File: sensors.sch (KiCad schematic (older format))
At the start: 9 parts, among them J3 Screw_Terminal_01x08, J4 Screw_Terminal_01x08, J7 Screw_Terminal_01x02, J8 Conn_01x02_Male, U2 LTC2449CUHF, U4 INA126U

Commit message: completed design 2.0
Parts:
- removed J7: Screw_Terminal_01x02, TerminalBlock_Phoenix:TerminalBlock_Phoenix_MKDS-1,5-2-5.08_1x02_P5.08mm_Horizontal, symbol Connector:Screw_Terminal_01x02
- removed J8: Conn_01x02_Male, Connector_PinHeader_2.54mm:PinHeader_1x02_P2.54mm_Vertical, symbol Connector:Conn_01x02_Male
- added J7: Screw_Terminal_01x04, TerminalBlock_Phoenix:TerminalBlock_Phoenix_MKDS-1,5-4-5.08_1x04_P5.08mm_Horizontal, symbol Connector:Screw_Terminal_01x04
- added J8: Conn_01x03_Male, Connector_PinHeader_2.54mm:PinHeader_1x03_P2.54mm_Vertical, symbol Connector:Conn_01x03_Male
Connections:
- net +EXC: now also J7.1 (Pin_1), J8.1 (Pin_1)
- net GND: now also J7.4 (Pin_4)
- net LC: now also J8.2 (Pin_2)
- net LC+: now also J7.3 (Pin_3)
- net LC-: now also J7.2 (Pin_2)
- net SEN0: now also J8.3 (Pin_3)
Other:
- note added: "Allow shorting LC and SEN0"
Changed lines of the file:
@@
 Text GLabel 7800 2400 0    50   Input ~ 0
 LC-
+Text GLabel 10000 1250 0    50   Input ~ 0
+LC+
+Text GLabel 10000 1150 0    50   Input ~ 0
+LC-
+Text GLabel 10100 2100 0    50   Input ~ 0
++EXC
+Text GLabel 10100 2000 0    50   Input ~ 0
+LC
 $Comp
-L Connector:Screw_Terminal_01x02 J7
-U 1 1 5EEF2437
-P 10250 1150
-F 0 "J7" H 10330 1142 50  0000 L CNN
-F 1 "Screw_Terminal_01x02" H 10330 1051 50  0000 L CNN
-F 2 "TerminalBlock_Phoenix:TerminalBlock_Phoenix_MKDS-1,5-2-5.08_1x02_P5.08mm_Horizontal" H 10250 1150 50  0001 C CNN
-F 3 "~" H 10250 1150 50  0001 C CNN
-	1    10250 1150
+L Connector:Conn_01x03_Male J8
+U 1 1 5EF5E577
+P 10300 2000
+F 0 "J8" H 10272 1932 50  0000 R CNN
+F 1 "Conn_01x03_Male" H 10272 2023 50  0000 R CNN
+F 2 "Connector_PinHeader_2.54mm:PinHeader_1x03_P2.54mm_Vertical" H 10300 2000 50  0001 C CNN
+F 3 "~" H 10300 2000 50  0001 C CNN
+	1    10300 2000
+	-1   0    0    1
+$EndComp
+Text GLabel 10100 1900 0    50   Input ~ 0
+SEN0
+Text Notes 10900 1800 2    50   ~ 0
+Allow shorting LC and SEN0
+$Comp
+L Connector:Screw_Terminal_01x04 J7
+U 1 1 5EF619ED
+P 10200 1150
+F 0 "J7" H 10280 1142 50  0000 L CNN
+F 1 "Screw_Terminal_01x04" H 10280 1051 50  0000 L CNN
+F 2 "TerminalBlock_Phoenix:TerminalBlock_Phoenix_MKDS-1,5-4-5.08_1x04_P5.08mm_Horizontal" H 10200 1150 50  0001 C CNN
+F 3 "~" H 10200 1150 50  0001 C CNN
+	1    10200 1150
 	1    0    0    -1
 $EndComp
-$Comp
-L Connector:Conn_01x02_Male J8
-U 1 1 5EEF4A47
-P 10250 1750
-F 0 "J8" H 10222 1632 50  0000 R CNN
-F 1 "Conn_01x02_Male" H 10222 1723 50  0000 R CNN
-F 2 "Connector_PinHeader_2.54mm:PinHeader_1x02_P2.54mm_Vertical" H 10250 1750 50  0001 C CNN
-F 3 "~" H 10250 1750 50  0001 C CNN
-	1    10250 1750
-	-1   0    0    1
-$EndComp
-Text GLabel 10050 1150 0    50   Input ~ 0
-LC+
-Text GLabel 10050 1250 0    50   Input ~ 0
-LC-
-Text GLabel 10050 1650 0    50   Input ~ 0
+Text GLabel 10000 1050 0    50   Input ~ 0
 +EXC
-Text GLabel 10050 1750 0    50   Input ~ 0
-LC
+Text GLabel 10000 1350 0    50   Input ~ 0
+GND
 $EndSCHEMATC

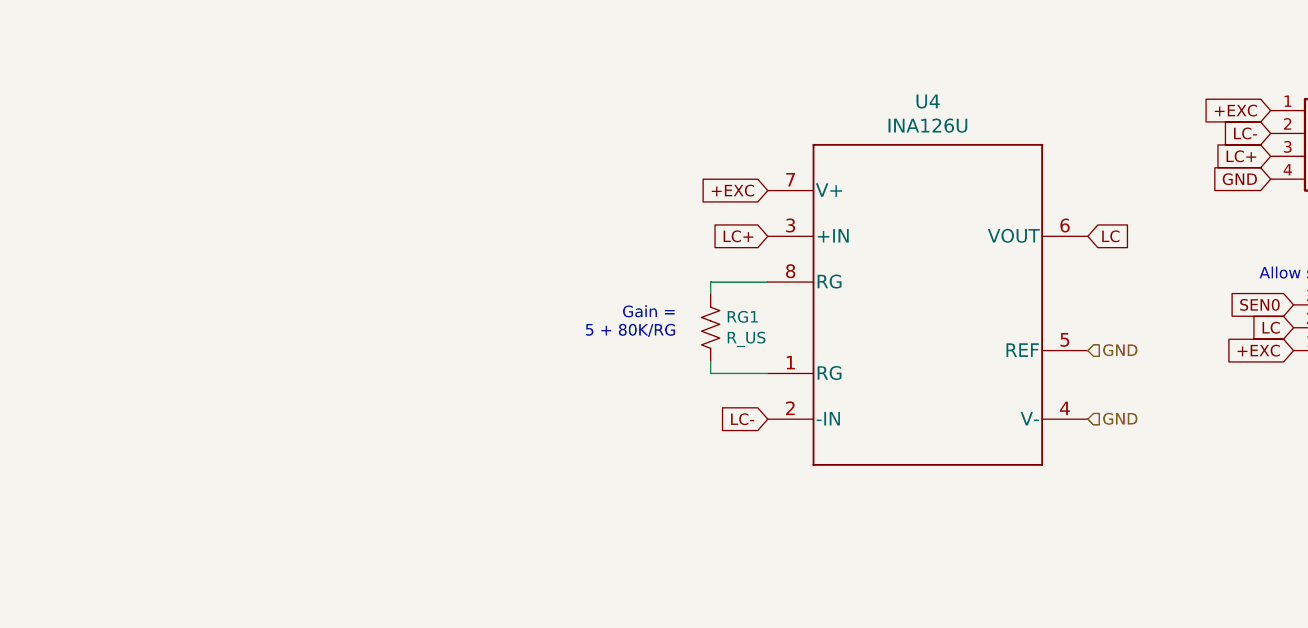
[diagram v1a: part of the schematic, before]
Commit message: added low pass filter to load cell inputs
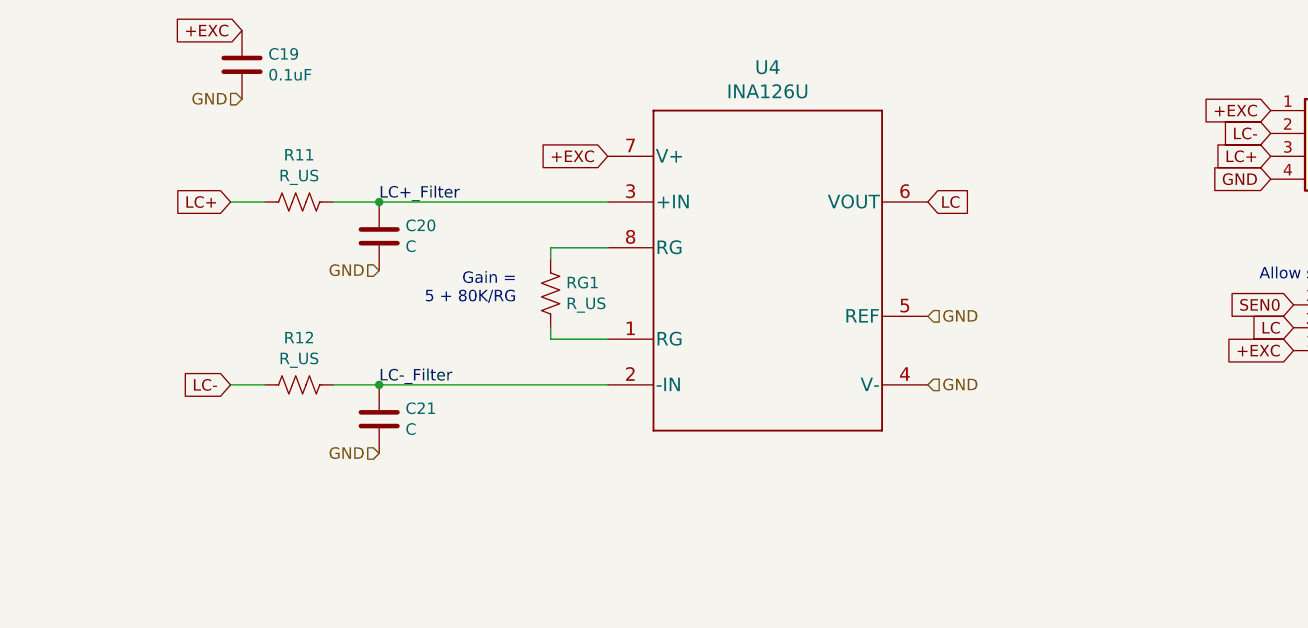
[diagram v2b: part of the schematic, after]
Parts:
- added C19: 0.1uF, Capacitor_SMD:C_0805_2012Metric_Pad1.15x1.40mm_HandSolder, symbol Device:C
- added C20, C21: C, Capacitor_SMD:C_0805_2012Metric_Pad1.15x1.40mm_HandSolder, symbol Device:C
- added R11, R12: R_US, Resistor_SMD:R_0805_2012Metric_Pad1.15x1.40mm_HandSolder, symbol Device:R_US
- RG1: footprint Resistor_THT:R_Axial_DIN0204_L3.6mm_D1.6mm_P7.62mm_Horizontal -> Resistor_THT:R_Axial_DIN0309_L9.0mm_D3.2mm_P12.70mm_Horizontal
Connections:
- net +EXC: now also C19.1
- net GND: now also C19.2, C20.2, C21.2
- net LC+: now also R11.2; no longer U4.3 (+IN)
- net LC-: now also R12.2; no longer U4.2 (-IN)
- new net LC+_Filter: C20.1, R11.1, U4.3 (+IN)
- new net LC-_Filter: C21.1, R12.1, U4.2 (-IN)
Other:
- moved on the sheet: RG1, U4
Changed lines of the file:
@@
 L INA126U:INA126U U4
 U 1 1 5EED8A04
-P 8500 1900
-F 0 "U4" H 8500 2788 60  0000 C CNN
-F 1 "INA126U" H 8500 2682 60  0000 C CNN
-F 2 "footprints:INA126U" H 8500 1840 60  0001 C CNN
-F 3 "" H 8500 1900 60  0000 C CNN
-	1    8500 1900
+P 7800 1750
+F 0 "U4" H 7800 2638 60  0000 C CNN
+F 1 "INA126U" H 7800 2532 60  0000 C CNN
+F 2 "footprints:INA126U" H 7800 1690 60  0001 C CNN
+F 3 "" H 7800 1750 60  0000 C CNN
+	1    7800 1750
 	1    0    0    -1
 $EndComp
-Text GLabel 7800 1400 0    50   Input ~ 0
+Text GLabel 7100 1250 0    50   Input ~ 0
 +EXC
-Text HLabel 9200 2100 2    50   Input ~ 0
+Text HLabel 8500 1950 2    50   Input ~ 0
 GND
-Text HLabel 9200 2400 2    50   Input ~ 0
+Text HLabel 8500 2250 2    50   Input ~ 0
 GND
 $Comp
 L Device:R_US RG1
 U 1 1 5EEEE283
-P 7550 2000
-F 0 "RG1" H 7618 2046 50  0000 L CNN
-F 1 "R_US" H 7618 1955 50  0000 L CNN
-F 2 "Resistor_THT:R_Axial_DIN0204_L3.6mm_D1.6mm_P7.62mm_Horizontal" V 7590 1990 50  0001 C CNN
-F 3 "~" H 7550 2000 50  0001 C CNN
-	1    7550 2000
+P 6850 1850
+F 0 "RG1" H 6918 1896 50  0000 L CNN
+F 1 "R_US" H 6918 1805 50  0000 L CNN
+F 2 "Resistor_THT:R_Axial_DIN0309_L9.0mm_D3.2mm_P12.70mm_Horizontal" V 6890 1840 50  0001 C CNN
+F 3 "~" H 6850 1850 50  0001 C CNN
+	1    6850 1850
 	1    0    0    -1
 $EndComp
 Wire Wire Line
-	7800 1800 7550 1800
+	7100 1650 6850 1650
 Wire Wire Line
-	7550 1800 7550 1850
+	6850 1650 6850 1700
 Wire Wire Line
-	7550 2150 7550 2200
+	6850 2000 6850 2050
 Wire Wire Line
-	7550 2200 7800 2200
-Text Notes 7400 2050 2    50   ~ 0
+	6850 2050 7100 2050
+Text Notes 6700 1900 2    50   ~ 0
 Gain =\n5 + 80K/RG
-Text GLabel 9200 1600 2    50   Input ~ 0
+Text GLabel 8500 1450 2    50   Input ~ 0
 LC
-Text GLabel 7800 1600 0    50   Input ~ 0
-LC+
-Text GLabel 7800 2400 0    50   Input ~ 0
+Text GLabel 5450 2250 0    50   Input ~ 0
 LC-
 Text GLabel 10000 1250 0    50   Input ~ 0
@@
 Text GLabel 10000 1350 0    50   Input ~ 0
 GND
+$Comp
+L Device:C C19
+U 1 1 5EDBC2A8
+P 5500 850
+F 0 "C19" H 5615 896 50  0000 L CNN
+F 1 "0.1uF" H 5615 805 50  0000 L CNN
+F 2 "Capacitor_SMD:C_0805_2012Metric_Pad1.15x1.40mm_HandSolder" H 5538 700 50  0001 C CNN
+F 3 "~" H 5500 850 50  0001 C CNN
+F 4 "ceramic" H 5500 850 50  0001 C CNN "dielectric"
+	1    5500 850
+	1    0    0    -1
+$EndComp
+Text GLabel 5500 700  0    50   Input ~ 0
++EXC
+Text HLabel 5500 1000 0    50   Input ~ 0
+GND
+$Comp
+L Device:R_US R12
+U 1 1 5EDB4E17
+P 5750 2250
+F 0 "R12" V 5545 2250 50  0000 C CNN
+F 1 "R_US" V 5636 2250 50  0000 C CNN
+F 2 "Resistor_SMD:R_0805_2012Metric_Pad1.15x1.40mm_HandSolder" V 5790 2240 50  0001 C CNN
+F 3 "~" H 5750 2250 50  0001 C CNN
+	1    5750 2250
+	0    1    1    0
+$EndComp
+$Comp
+L Device:C C21
+U 1 1 5EDB5BF7
+P 6100 2400
+F 0 "C21" H 6215 2446 50  0000 L CNN
+F 1 "C" H 6215 2355 50  0000 L CNN
+F 2 "Capacitor_SMD:C_0805_2012Metric_Pad1.15x1.40mm_HandSolder" H 6138 2250 50  0001 C CNN
+F 3 "~" H 6100 2400 50  0001 C CNN
+	1    6100 2400
+	1    0    0    -1
+$EndComp
+Text HLabel 6100 2550 0    50   Input ~ 0
+GND
+Wire Wire Line
+	5450 2250 5600 2250
+Wire Wire Line
+	5900 2250 6100 2250
+Connection ~ 6100 2250
+Text GLabel 5450 1450 0    50   Input ~ 0
+LC+
+$Comp
+L Device:R_US R11
+U 1 1 5EDBBFC4
+P 5750 1450
+F 0 "R11" V 5545 1450 50  0000 C CNN
+F 1 "R_US" V 5636 1450 50  0000 C CNN
+F 2 "Resistor_SMD:R_0805_2012Metric_Pad1.15x1.40mm_HandSolder" V 5790 1440 50  0001 C CNN
+F 3 "~" H 5750 1450 50  0001 C CNN
+	1    5750 1450
+	0    1    1    0
+$EndComp
+$Comp
+L Device:C C20
+U 1 1 5EDBBFCA
+P 6100 1600
+F 0 "C20" H 6215 1646 50  0000 L CNN
+F 1 "C" H 6215 1555 50  0000 L CNN
+F 2 "Capacitor_SMD:C_0805_2012Metric_Pad1.15x1.40mm_HandSolder" H 6138 1450 50  0001 C CNN
+F 3 "~" H 6100 1600 50  0001 C CNN
+	1    6100 1600
+	1    0    0    -1
+$EndComp
+Text HLabel 6100 1750 0    50   Input ~ 0
+GND
+Wire Wire Line
+	5450 1450 5600 1450
+Wire Wire Line
+	5900 1450 6100 1450
+Connection ~ 6100 1450
+Wire Wire Line
+	6100 1450 7100 1450
+Wire Wire Line
+	6100 2250 7100 2250
+Text Label 6100 1450 0    50   ~ 0
+LC+_Filter
+Text Label 6100 2250 0    50   ~ 0
+LC-_Filter
 $EndSCHEMATC
